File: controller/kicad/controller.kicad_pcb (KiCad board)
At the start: 2 copper layers, 90 x 88.4 mm, 40 parts, among them J1 pcie_98, J2 USB_C_Receptacle_USB2.0, SW2 D2F-01F-A, U1 WeAct_STM32H750_Module, U10 ESD5344D, U11 ESD5344D, U12 ESD5344D, U13 ESD5344D, U14 ESD5344D, U15 ESD5344D, U16 CP2102N-A02-GQFN28R, U17 ESD5344D, U2 ESD5344D, U3 ESD5344D, U4 ESD5344D, U5 ESD5344D, U6 ESD5344D, U7 ESD5344D, U8 ESD5344D, U9 ESD5344D

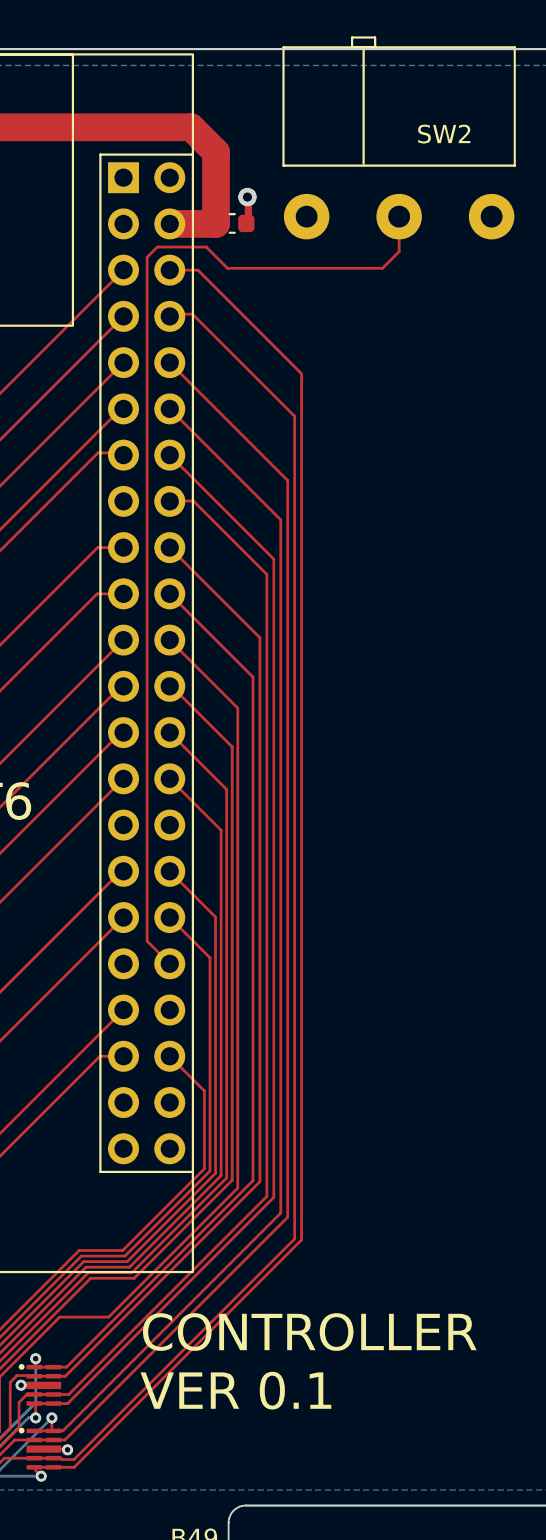
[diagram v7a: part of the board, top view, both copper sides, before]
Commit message: Generated JLCPCB production files.
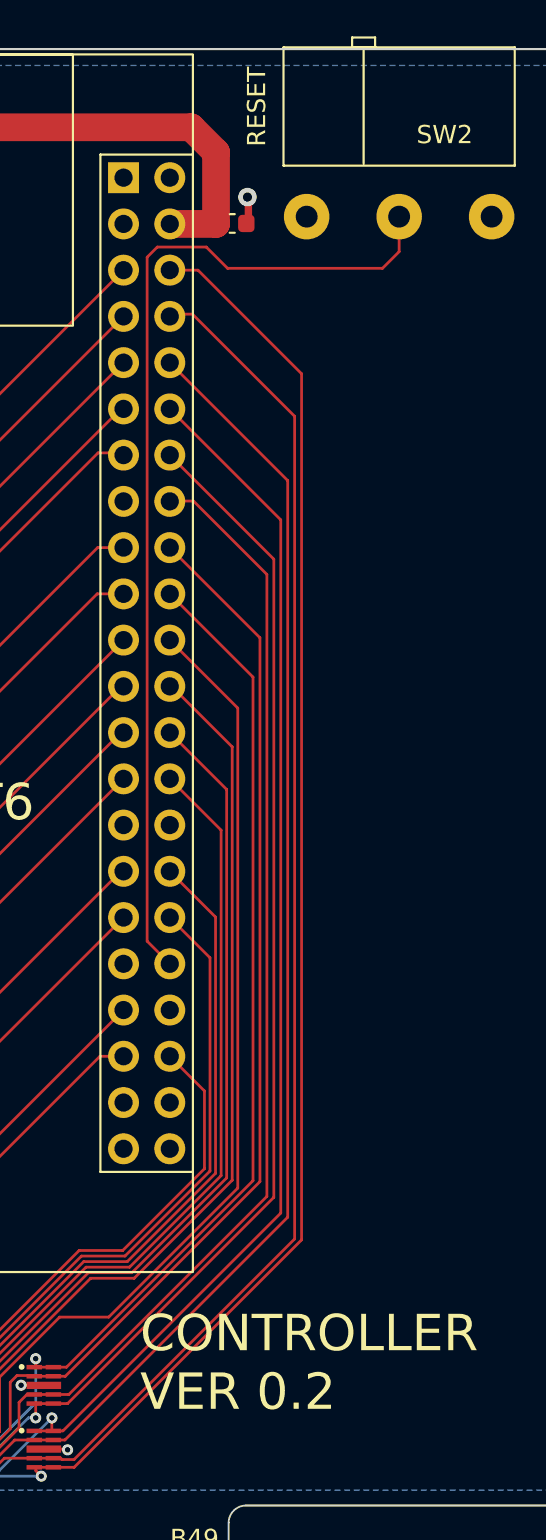
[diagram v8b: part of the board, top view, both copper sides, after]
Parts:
- D2: value LED YELLOW -> YELLOW_LED
- D3: value LED_GREEN -> GREEN LED
- JP1: footprint Connector_PinHeader_2.54mm:PinHeader_1x02_P2.54mm_Vertical -> controller:PinHeader_1x02_P2.54mm_Vertical
- R9: value 5K1 -> 10K
- moved JP1 1.27 mm to (54.0, 0.76), turned to -90 degrees
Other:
- board text added: "CONTROLLER VER 0.2"
- board text added: "RESET"
- board text removed: "CONTROLLER VER 0.1"
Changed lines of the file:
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@@
         (effects (font (size 1 1) (thickness 0.15)))
+    )
+    (fp_text user "USB" (at -9.525 -29.464 unlocked) (layer "F.SilkS")
+        (effects (font (size 1 1) (thickness 0.15)) (justify left bottom))
     )
     (fp_text user "SD" (at 5.461 -29.464 unlocked) (layer "F.SilkS")
         (effects (font (size 1 1) (thickness 0.15)) (justify left bottom))
     )
-    (fp_text user "USB" (at -9.525 -29.464 unlocked) (layer "F.SilkS")
-        (effects (font (size 1 1) (thickness 0.15)) (justify left bottom))
+    (fp_text user "${REFERENCE}" (at 17.78 0 90) (layer "F.Fab")
+        (effects (font (size 1 1) (thickness 0.15)))
     )
     (fp_text user "${REFERENCE}" (at -17.78 0 90) (layer "F.Fab")
-        (effects (font (size 1 1) (thickness 0.15)))
-    )
-    (fp_text user "${REFERENCE}" (at 17.78 0 90) (layer "F.Fab")
         (effects (font (size 1 1) (thickness 0.15)))
     )
@@
         (effects (font (size 1 1) (thickness 0.15)))
     )
-    (fp_text value "LED_GREEN" (at 0 1.43) (layer "F.Fab")
+    (fp_text value "GREEN LED" (at 0 1.43) (layer "F.Fab")
         (effects (font (size 1 1) (thickness 0.15)))
     )
@@
         (effects (font (size 1 1) (thickness 0.15)))
     )
+    (fp_text user "A1" (at -10.06 -6 unlocked) (layer "B.SilkS")
+        (effects (font (size 1 1) (thickness 0.15)) (justify left bottom mirror))
+    )
     (fp_text user "A49" (at 38.73 -6 unlocked) (layer "B.SilkS")
-        (effects (font (size 1 1) (thickness 0.15)) (justify left bottom mirror))
-    )
-    (fp_text user "A1" (at -10.06 -6 unlocked) (layer "B.SilkS")
         (effects (font (size 1 1) (thickness 0.15)) (justify left bottom mirror))
     )
@@
     )
   )
-  (footprint "Connector_PinHeader_2.54mm:PinHeader_1x02_P2.54mm_Vertical" (layer "F.Cu")
-    (at 54.0258 -0.513)
+  (footprint "controller:PinHeader_1x02_P2.54mm_Vertical" (layer "F.Cu")
+    (at 54.0258 0.757 -90)
     (descr "Through hole straight pin header, 1x02, 2.54mm pitch, single row")
     (tags "Through hole pin header THT 1x02 2.54mm single row")
@@
     (property "ki_keywords" "Jumper SPST")
     (attr through_hole)
-    (fp_text reference "JP1" (at 0.1778 5.4152) (layer "F.SilkS") hide
-        (effects (font (size 1 1) (thickness 0.15)))
-    )
-    (fp_text value "Jumper_2_Open" (at 0 4.87) (layer "F.Fab")
-        (effects (font (size 1 1) (thickness 0.15)))
-    )
-    (fp_text user "${REFERENCE}" (at 0 1.27 90) (layer "F.Fab")
-        (effects (font (size 1 1) (thickness 0.15)))
-    )
-    (fp_line (start -1.33 -1.33) (end 0 -1.33)
-      (stroke (width 0.12) (type solid)) (layer "F.SilkS"))
-    (fp_line (start -1.33 0) (end -1.33 -1.33)
-      (stroke (width 0.12) (type solid)) (layer "F.SilkS"))
-    (fp_line (start -1.33 1.27) (end -1.33 3.87)
-      (stroke (width 0.12) (type solid)) (layer "F.SilkS"))
-    (fp_line (start -1.33 1.27) (end 1.33 1.27)
-      (stroke (width 0.12) (type solid)) (layer "F.SilkS"))
-    (fp_line (start -1.33 3.87) (end 1.33 3.87)
-      (stroke (width 0.12) (type solid)) (layer "F.SilkS"))
-    (fp_line (start 1.33 1.27) (end 1.33 3.87)
-      (stroke (width 0.12) (type solid)) (layer "F.SilkS"))
-    (fp_line (start -1.8 -1.8) (end -1.8 4.35)
-      (stroke (width 0.05) (type solid)) (layer "F.CrtYd"))
-    (fp_line (start -1.8 4.35) (end 1.8 4.35)
-      (stroke (width 0.05) (type solid)) (layer "F.CrtYd"))
-    (fp_line (start 1.8 -1.8) (end -1.8 -1.8)
-      (stroke (width 0.05) (type solid)) (layer "F.CrtYd"))
-    (fp_line (start 1.8 4.35) (end 1.8 -1.8)
-      (stroke (width 0.05) (type solid)) (layer "F.CrtYd"))
-    (fp_line (start -1.27 -0.635) (end -0.635 -1.27)
-      (stroke (width 0.1) (type solid)) (layer "F.Fab"))
-    (fp_line (start -1.27 3.81) (end -1.27 -0.635)
-      (stroke (width 0.1) (type solid)) (layer "F.Fab"))
-    (fp_line (start -0.635 -1.27) (end 1.27 -1.27)
-      (stroke (width 0.1) (type solid)) (layer "F.Fab"))
-    (fp_line (start 1.27 -1.27) (end 1.27 3.81)
-      (stroke (width 0.1) (type solid)) (layer "F.Fab"))
-    (fp_line (start 1.27 3.81) (end -1.27 3.81)
-      (stroke (width 0.1) (type solid)) (layer "F.Fab"))
-    (pad "1" thru_hole rect (at 0 0) (size 1.7 1.7) (drill 1) (layers "*.Cu" "*.Mask")
+    (fp_text reference "JP1" (at -3.6 0) (layer "F.SilkS") hide
+        (effects (font (size 1 1) (thickness 0.15)))
+    )
+    (fp_text value "Jumper_2_Open" (at 0 4.87 90) (layer "F.Fab")
+        (effects (font (size 1 1) (thickness 0.15)))
+    )
+    (fp_text user "${REFERENCE}" (at 0 1.27) (layer "F.Fab")
+        (effects (font (size 1 1) (thickness 0.15)))
+    )
+    (fp_line (start -2.6 1.33) (end -2.6 0)
+      (stroke (width 0.12) (type solid)) (layer "F.SilkS"))
+    (fp_line (start -1.27 1.33) (end -2.6 1.33)
+      (stroke (width 0.12) (type solid)) (layer "F.SilkS"))
+    (fp_line (start 0 -1.33) (end 2.6 -1.33)
+      (stroke (width 0.12) (type solid)) (layer "F.SilkS"))
+    (fp_line (start 0 1.33) (end 0 -1.33)
+      (stroke (width 0.12) (type solid)) (layer "F.SilkS"))
+    (fp_line (start 0 1.33) (end 2.6 1.33)
+      (stroke (width 0.12) (type solid)) (layer "F.SilkS"))
+    (fp_line (start 2.6 1.33) (end 2.6 -1.33)
+      (stroke (width 0.12) (type solid)) (layer "F.SilkS"))
+    (fp_line (start -3.07 -1.8) (end -3.07 1.8)
+      (stroke (width 0.05) (type solid)) (layer "F.CrtYd"))
+    (fp_line (start -3.07 1.8) (end 3.08 1.8)
+      (stroke (width 0.05) (type solid)) (layer "F.CrtYd"))
+    (fp_line (start 3.08 -1.8) (end -3.07 -1.8)
+      (stroke (width 0.05) (type solid)) (layer "F.CrtYd"))
+    (fp_line (start 3.08 1.8) (end 3.08 -1.8)
+      (stroke (width 0.05) (type solid)) (layer "F.CrtYd"))
+    (fp_line (start -2.54 -1.27) (end 2.54 -1.27)
+      (stroke (width 0.1) (type solid)) (layer "F.Fab"))
+    (fp_line (start -2.54 0.635) (end -2.54 -1.27)
+      (stroke (width 0.1) (type solid)) (layer "F.Fab"))
+    (fp_line (start -1.905 1.27) (end -2.54 0.635)
+      (stroke (width 0.1) (type solid)) (layer "F.Fab"))
+    (fp_line (start 2.54 -1.27) (end 2.54 1.27)
+      (stroke (width 0.1) (type solid)) (layer "F.Fab"))
+    (fp_line (start 2.54 1.27) (end -1.905 1.27)
+      (stroke (width 0.1) (type solid)) (layer "F.Fab"))
+    (pad "1" thru_hole rect (at -1.27 0) (size 1.7 1.7) (drill 1) (layers "*.Cu" "*.Mask")
       (net 41 "/PA10") (pinfunction "A") (pintype "passive"))
-    (pad "2" thru_hole oval (at 0 2.54) (size 1.7 1.7) (drill 1) (layers "*.Cu" "*.Mask")
+    (pad "2" thru_hole oval (at 1.27 0) (size 1.7 1.7) (drill 1) (layers "*.Cu" "*.Mask")
       (net 35 "/PA9") (pinfunction "B") (pintype "passive"))
     (model "${KICAD6_3DMODEL_DIR}/Connector_PinHeader_2.54mm.3dshapes/PinHeader_1x02_P2.54mm_Vertical.wrl"
@@
     (descr "Resistor SMD 0603 (1608 Metric), square (rectangular) end terminal, IPC_7351 nominal, (Body size source: IPC-SM-782 page 72, https://www.pcb-3d.com/wordpress/wp-content/uploads/ipc-sm-782a_amendment_1_and_2.pdf), generated with kicad-footprint-generator")
     (tags "resistor")
-    (property "LCSC" "C23186")
+    (property "LCSC" "C25744")
     (property "Sheetfile" "controller.kicad_sch")
     (property "Sheetname" "")
@@
         (effects (font (size 1 1) (thickness 0.15)))
     )
-    (fp_text value "5K1" (at 0 1.43) (layer "F.Fab")
+    (fp_text value "10K" (at 0 1.43) (layer "F.Fab")
         (effects (font (size 1 1) (thickness 0.15)))
     )
@@
         (effects (font (size 1 1) (thickness 0.15)))
     )
-    (fp_text value "LED YELLOW" (at 0 1.43) (layer "F.Fab")
+    (fp_text value "YELLOW_LED" (at 0 1.43) (layer "F.Fab")
         (effects (font (size 1 1) (thickness 0.15)))
     )
@@
       (net 150 "/NRST") (pinfunction "2") (pintype "passive"))
     (model "${KIPRJMOD}/3d_models/Microswitch - Omron D2F-L-A.stp"
-      (offset (xyz 5.08 5.715 2.921))
+      (offset (xyz 0 5.71 2.921))
       (scale (xyz 1 1 1))
       (rotate (xyz 0 0 0))
@@
     (effects (font (size 2 2) (thickness 0.3)) (justify left bottom))
   )
-  (gr_text "CONTROLLER\nVER 0.1" (at 104.2924 46.5328) (layer "F.SilkS")
+  (gr_text "CONTROLLER\nVER 0.2" (at 104.2924 46.5328) (layer "F.SilkS")
     (effects (font (size 2 2) (thickness 0.2)) (justify left bottom))
   )
@@
     (effects (font (size 1 1) (thickness 0.15)) (justify left bottom))
   )
+  (gr_text "RESET" (at 111.2774 -23.0378 90) (layer "F.SilkS")
+    (effects (font (size 1 1) (thickness 0.15)) (justify left bottom))
+  )
